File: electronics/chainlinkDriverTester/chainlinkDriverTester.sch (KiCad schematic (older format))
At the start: 151 parts, among them J1 Barrel_Jack_Switch, J10 Sensor C, J11 Sensor D, J12 Motor E, J13 Motor F, J14 Sensor E, J15 Sensor F, J2 Conn_01x03_Female, J22 Power, J26 exp, J27 exp, J28 exp, J29 exp, J3 Motor A, J30 exp, J31 exp, J32 Conn_01x06_Female, J5 Motor B, J6 Motor C, J7 Motor D, J8 Sensor A, J9 Sensor B, U1 AP7361C-33E, U2 TTGO_TDisplay, U3 VN7007ALH, U4 MCP23017_SS, U5 INA219BxD, U6 SN74LV1T34DBV, U7 Buck

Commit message: Updates
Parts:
- removed C3: 100uF, Capacitor_SMD:CP_Elec_8x10, symbol Device:CP_Small
- added Z101: Fuse, Dummy:Dummy, symbol no_pin:no_pin
- C1, C5: DK# (none) -> 732-8430-1-ND
- C10, C6, C7, C8, C9: DK# (none) -> 1276-2449-1-ND
- C2, C4: DK# (none) -> 1276-1244-1-ND
- D1, D2, D4: footprint LED_SMD:LED_0805_2012Metric -> ModifiedSymbols:LED_0805_2012Metric_Silkscreen; DK# (none) -> 475-1278-1-ND
- D3, D7: value 1N5819 -> 2A 500mV; footprint Diode_SMD:D_SOD-123 -> Diode_SMD:D_SOD-128; DK# (none) -> 1727-1730-1-ND
- J1: DK# (none) -> 839-1514-ND
- J22: footprint ScrewTerminals:C8465_WJ500V-5.08-2P -> ScrewTerminals:Generic-5.08-2P; DK# (none) -> EB147A-02-D
- R1, R2, R8: DK# (none) -> RMCF0805JT1K00CT-ND
- R10, R3, R4, R5, R6: DK# (none) -> RMCF0805JT15K0CT-ND
- R11, R13, R7: DK# (none) -> RMCF0805JT220RCT-ND
- R9: DK# (none) -> RMCF0805JT2K00CT-ND
- U1: DK# (none) -> AP7361C-33E-13DICT-ND
- U3: DK# (none) -> 497-16868-1-ND
- U6: DK# (none) -> 296-37176-1-ND
- U7: footprint Buck:BuckModule -> Buck:BuckModuleBackSilk
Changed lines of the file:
@@
 	4950 2300 5700 2300
 $Comp
-L Device:CP_Small C3
-U 1 1 60F564AB
-P 2800 1050
-F 0 "C3" H 2888 1096 50  0000 L CNN
-F 1 "100uF" H 2888 1005 50  0000 L CNN
-F 2 "Capacitor_SMD:CP_Elec_8x10" H 2800 1050 50  0001 C CNN
-F 3 "~" H 2800 1050 50  0001 C CNN
-F 4 "C176665" H 2800 1050 50  0001 C CNN "LCSC"
-F 5 "0;0;180" H 2800 1050 50  0001 C CNN "JLCPCB_CORRECTION"
-	1    2800 1050
-	1    0    0    -1
-$EndComp
-$Comp
 L power:+12V #PWR015
 U 1 1 60F5782B
@@
 $EndComp
 $Comp
-L power:GND #PWR016
-U 1 1 60F582C0
-P 2800 1200
-F 0 "#PWR016" H 2800 950 50  0001 C CNN
-F 1 "GND" H 2805 1027 50  0000 C CNN
-F 2 "" H 2800 1200 50  0001 C CNN
-F 3 "" H 2800 1200 50  0001 C CNN
-	1    2800 1200
-	1    0    0    -1
-$EndComp
-Wire Wire Line
-	2800 900  2800 950
-Wire Wire Line
-	2800 1150 2800 1200
-$Comp
 L power:GND #PWR04
 U 1 1 60FBE6C2
@@
 F 2 "Resistor_SMD:R_0805_2012Metric" H 6700 4000 50  0001 C CNN
 F 3 "~" H 6700 4000 50  0001 C CNN
+F 4 "RMCF0805JT1K00CT-ND" H 6700 4000 50  0001 C CNN "DK#"
 	1    6700 4000
 	1    0    0    -1
@@
 F 2 "Resistor_SMD:R_0805_2012Metric" H 7000 4000 50  0001 C CNN
 F 3 "~" H 7000 4000 50  0001 C CNN
+F 4 "RMCF0805JT1K00CT-ND" H 7000 4000 50  0001 C CNN "DK#"
 	1    7000 4000
 	1    0    0    -1
@@
 F 2 "Capacitor_SMD:C_0805_2012Metric" H 13250 6850 50  0001 C CNN
 F 3 "~" H 13250 6850 50  0001 C CNN
+F 4 "1276-2449-1-ND" H 13250 6850 50  0001 C CNN "DK#"
 	1    13250 6850
 	-1   0    0    1
@@
 F 0 "D1" V 13300 5100 50  0000 R CNN
 F 1 "Red" V 13200 5150 50  0000 R CNN
-F 2 "LED_SMD:LED_0805_2012Metric" V 13250 4950 50  0001 C CNN
+F 2 "ModifiedSymbols:LED_0805_2012Metric_Silkscreen" V 13250 4950 50  0001 C CNN
 F 3 "~" V 13250 4950 50  0001 C CNN
+F 4 "475-1278-1-ND" H 13250 4950 50  0001 C CNN "DK#"
 	1    13250 4950
 	0    -1   -1   0
@@
 F 2 "Resistor_SMD:R_0805_2012Metric" H 13250 5200 50  0001 C CNN
 F 3 "~" H 13250 5200 50  0001 C CNN
+F 4 "RMCF0805JT220RCT-ND" H 13250 5200 50  0001 C CNN "DK#"
 	1    13250 5200
 	-1   0    0    1
@@
 F 2 "Resistor_SMD:R_0805_2012Metric" H 13400 4800 50  0001 C CNN
 F 3 "~" H 13400 4800 50  0001 C CNN
+F 4 "RMCF0805JT15K0CT-ND" H 13400 4800 50  0001 C CNN "DK#"
 	1    13400 4800
 	0    1    1    0
@@
 F 2 "Resistor_SMD:R_0805_2012Metric" H 13850 5250 50  0001 C CNN
 F 3 "~" H 13850 5250 50  0001 C CNN
+F 4 "RMCF0805JT1K00CT-ND" H 13850 5250 50  0001 C CNN "DK#"
 	1    13850 5250
 	-1   0    0    1
@@
 F 2 "Resistor_SMD:R_0805_2012Metric" H 13650 5050 50  0001 C CNN
 F 3 "~" H 13650 5050 50  0001 C CNN
+F 4 "RMCF0805JT15K0CT-ND" H 13650 5050 50  0001 C CNN "DK#"
 	1    13650 5050
 	-1   0    0    1
@@
 F 0 "D2" V 15850 5300 50  0000 R CNN
 F 1 "Red" V 15750 5350 50  0000 R CNN
-F 2 "LED_SMD:LED_0805_2012Metric" V 15800 5150 50  0001 C CNN
+F 2 "ModifiedSymbols:LED_0805_2012Metric_Silkscreen" V 15800 5150 50  0001 C CNN
 F 3 "~" V 15800 5150 50  0001 C CNN
+F 4 "475-1278-1-ND" H 15800 5150 50  0001 C CNN "DK#"
 	1    15800 5150
 	0    -1   -1   0
@@
 F 2 "Resistor_SMD:R_0805_2012Metric" H 15800 5400 50  0001 C CNN
 F 3 "~" H 15800 5400 50  0001 C CNN
+F 4 "RMCF0805JT2K00CT-ND" H 15800 5400 50  0001 C CNN "DK#"
 	1    15800 5400
 	-1   0    0    1
@@
 F 2 "VN7007ALHTR:VN7007ALHTR" H 14450 4900 50  0001 C CNN
 F 3 "" H 14450 4900 50  0001 C CNN
+F 4 "497-16868-1-ND" H 14450 4900 50  0001 C CNN "DK#"
 	1    14450 4900
 	1    0    0    -1
@@
 P 14950 6750
 F 0 "D3" V 14996 6680 50  0000 R CNN
-F 1 "1N5819" V 14905 6680 50  0000 R CNN
-F 2 "Diode_SMD:D_SOD-123" V 14950 6750 50  0001 C CNN
+F 1 "2A 500mV" V 14905 6680 50  0000 R CNN
+F 2 "Diode_SMD:D_SOD-128" V 14950 6750 50  0001 C CNN
 F 3 "~" V 14950 6750 50  0001 C CNN
+F 4 "1727-1730-1-ND" H 14950 6750 50  0001 C CNN "DK#"
 	1    14950 6750
 	0    -1   -1   0
@@
 F 2 "Resistor_SMD:R_0805_2012Metric" H 14050 6050 50  0001 C CNN
 F 3 "~" H 14050 6050 50  0001 C CNN
+F 4 "RMCF0805JT220RCT-ND" H 14050 6050 50  0001 C CNN "DK#"
 	1    14050 6050
 	0    -1   -1   0
@@
 F 2 "Resistor_SMD:R_0805_2012Metric" H 12950 5050 50  0001 C CNN
 F 3 "~" H 12950 5050 50  0001 C CNN
+F 4 "RMCF0805JT15K0CT-ND" H 12950 5050 50  0001 C CNN "DK#"
 	1    12950 5050
 	-1   0    0    1
@@
 F 0 "J22" H 1680 842 50  0000 L CNN
 F 1 "Power" H 1680 751 50  0000 L CNN
-F 2 "ScrewTerminals:C8465_WJ500V-5.08-2P" H 1600 850 50  0001 C CNN
+F 2 "ScrewTerminals:Generic-5.08-2P" H 1600 850 50  0001 C CNN
 F 3 "~" H 1600 850 50  0001 C CNN
 F 4 "C8465" H 1600 850 50  0001 C CNN "LCSC"
 F 5 "2.40;0;0" H 1600 850 50  0001 C CNN "JLCPCB_CORRECTION"
+F 6 "EB147A-02-D" H 1600 850 50  0001 C CNN "DK#"
 	1    1600 850
 	1    0    0    -1
@@
 Wire Wire Line
 	1300 800  1300 850
-$Comp
-L power:+12V #PWR0122
-U 1 1 6165EC47
-P 2800 900
-F 0 "#PWR0122" H 2800 750 50  0001 C CNN
-F 1 "+12V" H 2815 1073 50  0000 C CNN
-F 2 "" H 2800 900 50  0001 C CNN
-F 3 "" H 2800 900 50  0001 C CNN
-	1    2800 900
-	1    0    0    -1
-$EndComp
 Text Label 4200 5000 2    50   ~ 0
 12V_TEST_FEED
@@
 F 2 "Package_TO_SOT_SMD:SOT-223-3_TabPin2" H 7350 1325 50  0001 C CIN
 F 3 "https://www.diodes.com/assets/Datasheets/AP7361C.pdf" H 7350 1050 50  0001 C CNN
+F 4 "AP7361C-33E-13DICT-ND" H 7350 1100 50  0001 C CNN "DK#"
 	1    7350 1100
 	1    0    0    -1
@@
 F 2 "Capacitor_SMD:C_0805_2012Metric" H 6700 1200 50  0001 C CNN
 F 3 "~" H 6700 1200 50  0001 C CNN
+F 4 "1276-1244-1-ND" H 6700 1200 50  0001 C CNN "DK#"
 	1    6700 1200
 	-1   0    0    1
@@
 F 2 "Capacitor_SMD:C_0805_2012Metric" H 7800 1200 50  0001 C CNN
 F 3 "~" H 7800 1200 50  0001 C CNN
+F 4 "1276-1244-1-ND" H 7800 1200 50  0001 C CNN "DK#"
 	1    7800 1200
 	-1   0    0    1
@@
 F 4 "C134721" H 6300 1200 50  0001 C CNN "LCSC"
 F 5 "0;0;180" H 6300 1200 50  0001 C CNN "JLCPCB_CORRECTION"
+F 6 "732-8430-1-ND" H 6300 1200 50  0001 C CNN "DK#"
 	1    6300 1200
 	1    0    0    -1
@@
 F 4 "C134721" H 8200 1200 50  0001 C CNN "LCSC"
 F 5 "0;0;180" H 8200 1200 50  0001 C CNN "JLCPCB_CORRECTION"
+F 6 "732-8430-1-ND" H 8200 1200 50  0001 C CNN "DK#"
 	1    8200 1200
 	1    0    0    -1
@@
 F 2 "Resistor_SMD:R_0805_2012Metric" H 6800 6300 50  0001 C CNN
 F 3 "~" H 6800 6300 50  0001 C CNN
+F 4 "RMCF0805JT15K0CT-ND" H 6800 6300 50  0001 C CNN "DK#"
 	1    6800 6300
 	-1   0    0    1
@@
 F 2 "Capacitor_SMD:C_0805_2012Metric" H 8200 5300 50  0001 C CNN
 F 3 "~" H 8200 5300 50  0001 C CNN
+F 4 "1276-2449-1-ND" H 8200 5300 50  0001 C CNN "DK#"
 	1    8200 5300
 	0    -1   -1   0
@@
 F 2 "Resistor_SMD:R_0805_2012Metric" H 6600 6800 50  0001 C CNN
 F 3 "~" H 6600 6800 50  0001 C CNN
+F 4 "RMCF0805JT15K0CT-ND" H 6600 6800 50  0001 C CNN "DK#"
 	1    6600 6800
 	1    0    0    -1
@@
 F 0 "D4" V 9350 1350 50  0000 R CNN
 F 1 "Red" V 9250 1400 50  0000 R CNN
-F 2 "LED_SMD:LED_0805_2012Metric" V 9300 1200 50  0001 C CNN
+F 2 "ModifiedSymbols:LED_0805_2012Metric_Silkscreen" V 9300 1200 50  0001 C CNN
 F 3 "~" V 9300 1200 50  0001 C CNN
+F 4 "475-1278-1-ND" H 9300 1200 50  0001 C CNN "DK#"
 	1    9300 1200
 	0    -1   -1   0
@@
 F 2 "Resistor_SMD:R_0805_2012Metric" H 9300 1450 50  0001 C CNN
 F 3 "~" H 9300 1450 50  0001 C CNN
+F 4 "RMCF0805JT220RCT-ND" H 9300 1450 50  0001 C CNN "DK#"
 	1    9300 1450
 	-1   0    0    1
@@
 F 2 "Package_TO_SOT_SMD:SOT-23-5" H 7200 8650 50  0001 C CNN
 F 3 "https://www.ti.com/lit/ds/symlink/sn74lv1t34.pdf" H 6150 8700 50  0001 C CNN
+F 4 "296-37176-1-ND" H 6550 8900 50  0001 C CNN "DK#"
 	1    6550 8900
 	1    0    0    -1
@@
 F 2 "Capacitor_SMD:C_0805_2012Metric" H 6200 8700 50  0001 C CNN
 F 3 "~" H 6200 8700 50  0001 C CNN
+F 4 "1276-2449-1-ND" H 6200 8700 50  0001 C CNN "DK#"
 	1    6200 8700
 	1    0    0    -1
@@
 F 2 "Capacitor_SMD:C_0805_2012Metric" H 7050 8700 50  0001 C CNN
 F 3 "~" H 7050 8700 50  0001 C CNN
+F 4 "1276-2449-1-ND" H 7050 8700 50  0001 C CNN "DK#"
 	1    7050 8700
 	1    0    0    -1
@@
 F 2 "Capacitor_SMD:C_0805_2012Metric" H 7850 8700 50  0001 C CNN
 F 3 "~" H 7850 8700 50  0001 C CNN
+F 4 "1276-2449-1-ND" H 7850 8700 50  0001 C CNN "DK#"
 	1    7850 8700
 	1    0    0    -1
@@
 F 2 "PJ-202A:PJ-202A" H 850 860 50  0001 C CNN
 F 3 "~" H 850 860 50  0001 C CNN
+F 4 "839-1514-ND" H 800 900 50  0001 C CNN "DK#"
 	1    800  900
 	1    0    0    -1
@@
 F 0 "U7" H 4387 1325 50  0000 C CNN
 F 1 "Buck" H 4387 1234 50  0000 C CNN
-F 2 "Buck:BuckModule" H 4350 1000 50  0001 C CNN
+F 2 "Buck:BuckModuleBackSilk" H 4350 1000 50  0001 C CNN
 F 3 "" H 4350 1000 50  0001 C CNN
 	1    4350 1000
@@
 P 5150 900
 F 0 "D7" H 5200 750 50  0000 R CNN
-F 1 "1N5819" H 5300 800 50  0000 R CNN
-F 2 "Diode_SMD:D_SOD-123" V 5150 900 50  0001 C CNN
+F 1 "2A 500mV" H 5300 800 50  0000 R CNN
+F 2 "Diode_SMD:D_SOD-128" V 5150 900 50  0001 C CNN
 F 3 "~" V 5150 900 50  0001 C CNN
+F 4 "1727-1730-1-ND" H 5150 900 50  0001 C CNN "DK#"
 	1    5150 900
 	-1   0    0    1
 $EndComp
+$Comp
+L no_pin:no_pin Z101
+U 1 1 60734BDC
+P 15400 3400
+F 0 "Z101" H 15400 3687 60  0000 C CNN
+F 1 "Fuse" H 15400 3581 60  0000 C CNN
+F 2 "Dummy:Dummy" H 15400 3400 60  0001 C CNN
+F 3 "" H 15400 3400 60  0001 C CNN
+F 4 "0297003.WXNV" H 15400 3400 50  0001 C CNN "DK#"
+	1    15400 3400
+	1    0    0    -1
+$EndComp
 $EndSCHEMATC

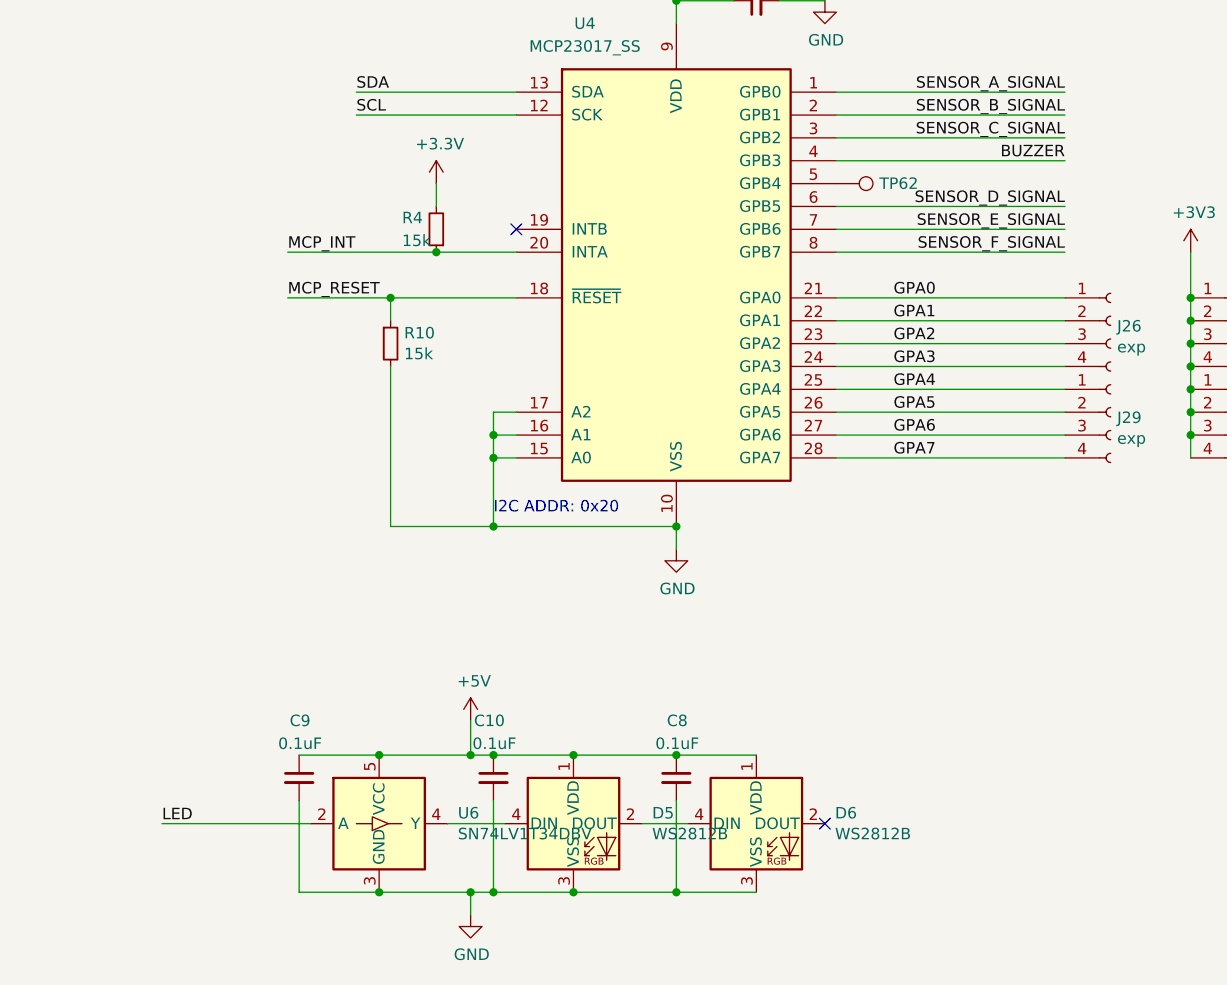
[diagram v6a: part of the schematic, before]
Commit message: chainlinkDriverTester: remove WS2812B LEDs, add detection switch
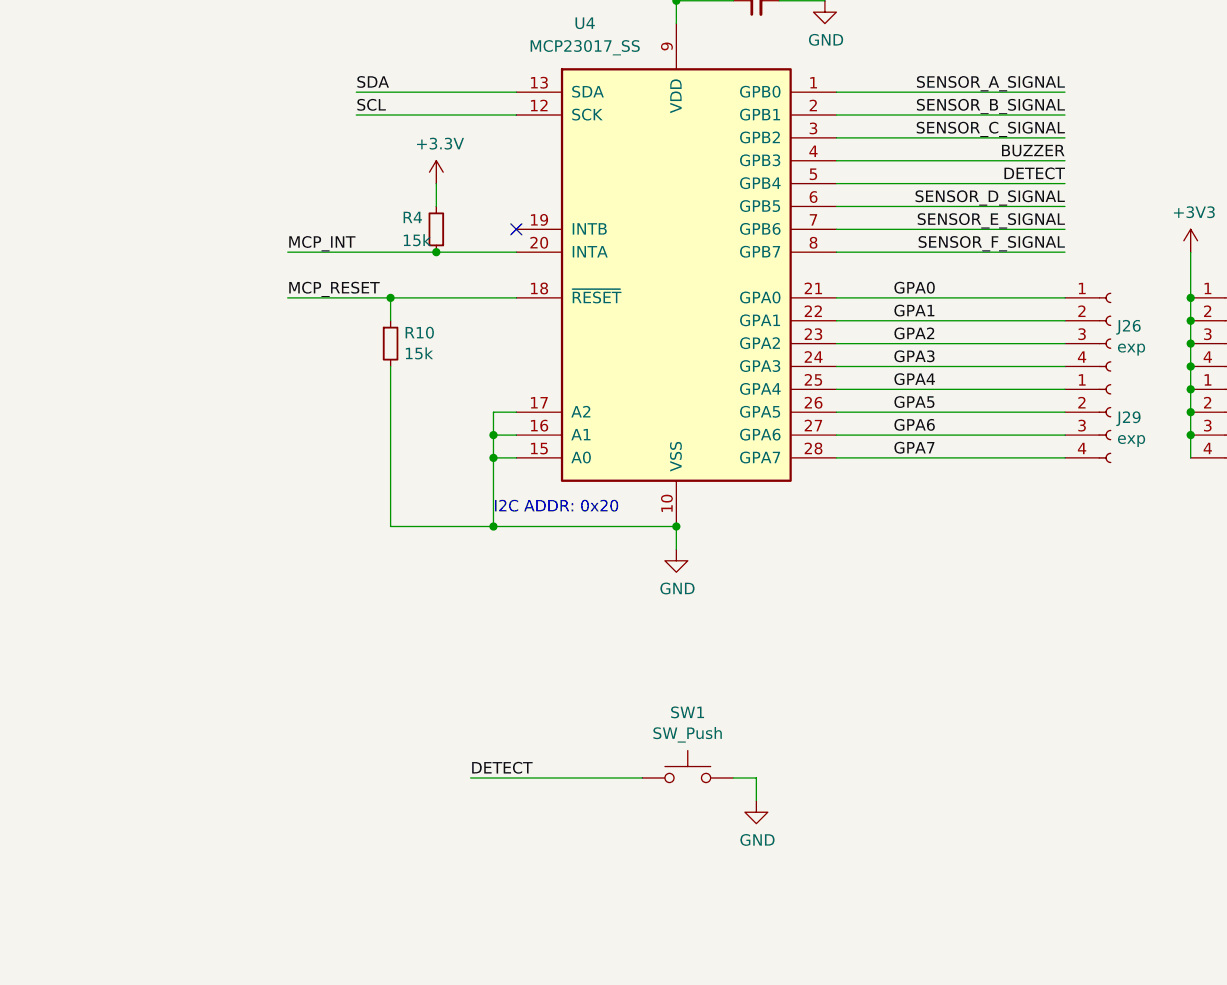
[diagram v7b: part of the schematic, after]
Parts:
- removed C10, C8, C9: 0.1uF, Capacitor_SMD:C_0805_2012Metric, symbol Device:C_Small
- removed D5, D6: WS2812B, LED_SMD:LED_WS2812B_PLCC4_5.0x5.0mm_P3.2mm, symbol LED:WS2812B
- removed TP62: TestPoint, TestPoint:TestPoint_THTPad_D2.0mm_Drill1.0mm, symbol Connector:TestPoint
- removed U6: SN74LV1T34DBV, Package_TO_SOT_SMD:SOT-23-5, symbol Logic_LevelTranslator:SN74LV1T34DBV
- added SW1: SW_Push, SwitchESE13:ESE13V01D, symbol Switch:SW_Push
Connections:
- net GND: now also SW1.2
- net DETECT: now reaches U4.5 (GPB4)
- net DETECT: now also SW1.1
- no-connect marks 19 -> 18
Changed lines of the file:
@@
 	1    0    0    -1
-$EndComp
-$Comp
-L Connector:TestPoint TP62
-U 1 1 61F7F830
-P 8550 6100
-F 0 "TP62" V 8550 6288 50  0000 L CNN
-F 1 "TestPoint" V 8595 6288 50  0001 L CNN
-F 2 "TestPoint:TestPoint_THTPad_D2.0mm_Drill1.0mm" H 8750 6100 50  0001 C CNN
-F 3 "~" H 8750 6100 50  0001 C CNN
-	1    8550 6100
-	0    1    1    0
 $EndComp
 Wire Wire Line
@@
 $EndComp
 $Comp
-L Logic_LevelTranslator:SN74LV1T34DBV U6
-U 1 1 6077F65C
-P 6550 8900
-F 0 "U6" H 6894 8946 50  0000 L CNN
-F 1 "SN74LV1T34DBV" H 6894 8855 50  0000 L CNN
-F 2 "Package_TO_SOT_SMD:SOT-23-5" H 7200 8650 50  0001 C CNN
-F 3 "https://www.ti.com/lit/ds/symlink/sn74lv1t34.pdf" H 6150 8700 50  0001 C CNN
-F 4 "296-37176-1-ND" H 6550 8900 50  0001 C CNN "DK#"
-	1    6550 8900
-	1    0    0    -1
-$EndComp
-$Comp
-L LED:WS2812B D5
-U 1 1 60781C6E
-P 7400 8900
-F 0 "D5" H 7744 8946 50  0000 L CNN
-F 1 "WS2812B" H 7744 8855 50  0000 L CNN
-F 2 "LED_SMD:LED_WS2812B_PLCC4_5.0x5.0mm_P3.2mm" H 7450 8600 50  0001 L TNN
-F 3 "https://cdn-shop.adafruit.com/datasheets/WS2812B.pdf" H 7500 8525 50  0001 L TNN
-	1    7400 8900
-	1    0    0    -1
-$EndComp
-Wire Wire Line
-	6850 8900 7100 8900
-$Comp
-L power:+5V #PWR03
-U 1 1 6079EC4F
-P 6950 8450
-F 0 "#PWR03" H 6950 8300 50  0001 C CNN
-F 1 "+5V" H 6965 8623 50  0000 C CNN
-F 2 "" H 6950 8450 50  0001 C CNN
-F 3 "" H 6950 8450 50  0001 C CNN
-	1    6950 8450
-	1    0    0    -1
-$EndComp
-$Comp
-L power:GND #PWR05
-U 1 1 6079F756
-P 6950 9300
-F 0 "#PWR05" H 6950 9050 50  0001 C CNN
-F 1 "GND" H 6955 9127 50  0000 C CNN
-F 2 "" H 6950 9300 50  0001 C CNN
-F 3 "" H 6950 9300 50  0001 C CNN
-	1    6950 9300
-	1    0    0    -1
-$EndComp
-Wire Wire Line
-	6550 9200 6950 9200
-Wire Wire Line
-	6950 9300 6950 9200
-Connection ~ 6950 9200
-Wire Wire Line
-	6950 9200 7050 9200
-Wire Wire Line
-	6550 8600 6950 8600
-Wire Wire Line
-	6950 8450 6950 8600
-Connection ~ 6950 8600
-Wire Wire Line
-	6950 8600 7050 8600
-Wire Wire Line
-	6250 8900 5600 8900
-Text Label 5600 8900 0    50   ~ 0
-LED
-$Comp
 L Connector:TestPoint TP71
 U 1 1 62B8767D
@@
 Text Label 1900 4900 0    50   ~ 0
 LED
-$Comp
-L LED:WS2812B D6
-U 1 1 60898405
-P 8200 8900
-F 0 "D6" H 8544 8946 50  0000 L CNN
-F 1 "WS2812B" H 8544 8855 50  0000 L CNN
-F 2 "LED_SMD:LED_WS2812B_PLCC4_5.0x5.0mm_P3.2mm" H 8250 8600 50  0001 L TNN
-F 3 "https://cdn-shop.adafruit.com/datasheets/WS2812B.pdf" H 8300 8525 50  0001 L TNN
-	1    8200 8900
-	1    0    0    -1
-$EndComp
-Wire Wire Line
-	7400 8600 7850 8600
-Connection ~ 7400 8600
-Connection ~ 7400 9200
-Wire Wire Line
-	7700 8900 7900 8900
-$Comp
-L Device:C_Small C?
-U 1 1 608F3043
-P 6200 8700
-AR Path="/60D00052/608F3043" Ref="C?"  Part="1"
-AR Path="/608F3043" Ref="C9"  Part="1"
-F 0 "C9" H 6250 8950 50  0000 R CNN
-F 1 "0.1uF" H 6300 8850 50  0000 R CNN
-F 2 "Capacitor_SMD:C_0805_2012Metric" H 6200 8700 50  0001 C CNN
-F 3 "~" H 6200 8700 50  0001 C CNN
-F 4 "1276-2449-1-ND" H 6200 8700 50  0001 C CNN "DK#"
-	1    6200 8700
-	1    0    0    -1
-$EndComp
-Wire Wire Line
-	6200 8600 6550 8600
-Connection ~ 6550 8600
-Wire Wire Line
-	6200 8800 6200 9200
-Wire Wire Line
-	6200 9200 6550 9200
-Connection ~ 6550 9200
-$Comp
-L Device:C_Small C?
-U 1 1 60932510
-P 7050 8700
-AR Path="/60D00052/60932510" Ref="C?"  Part="1"
-AR Path="/60932510" Ref="C10"  Part="1"
-F 0 "C10" H 7100 8950 50  0000 R CNN
-F 1 "0.1uF" H 7150 8850 50  0000 R CNN
-F 2 "Capacitor_SMD:C_0805_2012Metric" H 7050 8700 50  0001 C CNN
-F 3 "~" H 7050 8700 50  0001 C CNN
-F 4 "1276-2449-1-ND" H 7050 8700 50  0001 C CNN "DK#"
-	1    7050 8700
-	1    0    0    -1
-$EndComp
-Connection ~ 7050 8600
-Wire Wire Line
-	7050 8600 7400 8600
-Wire Wire Line
-	7050 8800 7050 9200
-Connection ~ 7050 9200
-Wire Wire Line
-	7050 9200 7400 9200
-$Comp
-L Device:C_Small C?
-U 1 1 60952141
-P 7850 8700
-AR Path="/60D00052/60952141" Ref="C?"  Part="1"
-AR Path="/60952141" Ref="C8"  Part="1"
-F 0 "C8" H 7900 8950 50  0000 R CNN
-F 1 "0.1uF" H 7950 8850 50  0000 R CNN
-F 2 "Capacitor_SMD:C_0805_2012Metric" H 7850 8700 50  0001 C CNN
-F 3 "~" H 7850 8700 50  0001 C CNN
-F 4 "1276-2449-1-ND" H 7850 8700 50  0001 C CNN "DK#"
-	1    7850 8700
-	1    0    0    -1
-$EndComp
-NoConn ~ 8500 8900
-Wire Wire Line
-	7400 9200 7850 9200
-Connection ~ 7850 8600
-Wire Wire Line
-	7850 8600 8200 8600
-Wire Wire Line
-	7850 8800 7850 9200
-Connection ~ 7850 9200
-Wire Wire Line
-	7850 9200 8200 9200
 NoConn ~ 2600 5200
 Text Label 8800 6600 0    50   ~ 0
@@
 	1    0    0    -1
 $EndComp
+$Comp
+L Switch:SW_Push SW1
+U 1 1 607D9BC7
+P 7900 8700
+F 0 "SW1" H 7900 8985 50  0000 C CNN
+F 1 "SW_Push" H 7900 8894 50  0000 C CNN
+F 2 "SwitchESE13:ESE13V01D" H 7900 8900 50  0001 C CNN
+F 3 "~" H 7900 8900 50  0001 C CNN
+F 4 "P13356SCT-ND" H 7900 8700 50  0001 C CNN "DK#"
+	1    7900 8700
+	1    0    0    -1
+$EndComp
+Wire Wire Line
+	7700 8700 6950 8700
+$Comp
+L power:GND #PWR0106
+U 1 1 6081A7BE
+P 8200 8800
+F 0 "#PWR0106" H 8200 8550 50  0001 C CNN
+F 1 "GND" H 8205 8627 50  0000 C CNN
+F 2 "" H 8200 8800 50  0001 C CNN
+F 3 "" H 8200 8800 50  0001 C CNN
+	1    8200 8800
+	1    0    0    -1
+$EndComp
+Wire Wire Line
+	8100 8700 8200 8700
+Wire Wire Line
+	8200 8700 8200 8800
+Text Label 6950 8700 0    50   ~ 0
+DETECT
+Wire Wire Line
+	9550 6100 8550 6100
+Text Label 9550 6100 2    50   ~ 0
+DETECT
 $EndSCHEMATC
